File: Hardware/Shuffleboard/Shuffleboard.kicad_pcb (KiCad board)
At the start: 4 copper layers, 131 x 132.4 mm, 31 parts, among them J1 1751138, J2 1751138, U1 COM-09032, U2 PAM8302AAS

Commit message: fet led driving
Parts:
- added D1: Red, LED_THT:LED_D5.0mm, F.Cu at (150.0, 98.5)
- added D32: Green, LED_THT:LED_D5.0mm, F.Cu at (221.2, 28.5)
- added IC1: DG3157EDL-T1-GE3, ShuffleboardFootprints:SOT65P210X110-6N, F.Cu at (157.8, 112.9)
- added IC2: DG3157EDL-T1-GE3, ShuffleboardFootprints:SOT65P210X110-6N, F.Cu at (162.3, 96.9)
- added Q1: NMOS, ShuffleboardFootprints:SOT95P260X110-3N, F.Cu at (145.7, 95.2)
- added R10: 500, Resistor_SMD:R_0603_1608Metric_Pad0.98x0.95mm_HandSolder, F.Cu at (145.8, 98.5)
- added R12: 10k, Resistor_SMD:R_0603_1608Metric_Pad0.98x0.95mm_HandSolder, F.Cu at (158.5, 94.2)
- added R13: 100k, Resistor_SMD:R_0603_1608Metric_Pad0.98x0.95mm_HandSolder, F.Cu at (152.2, 111.8)
- added R45: 10k, Resistor_SMD:R_0603_1608Metric_Pad0.98x0.95mm_HandSolder, F.Cu at (144.8, 114.5)
- added R8: 1k, Resistor_SMD:R_0603_1608Metric_Pad0.98x0.95mm_HandSolder, F.Cu at (227.8, 27.2)
- added R9: 10k, Resistor_SMD:R_0603_1608Metric_Pad0.98x0.95mm_HandSolder, F.Cu at (149.8, 114.5)
- added U3: LMV331, ShuffleboardFootprints:lmv331, F.Cu at (148.8, 108.7)
- J1, J2: value 1751138 -> 1869279; footprint ShuffleboardFootprints:1751138 -> ShuffleboardFootprints:1869279
- moved C6 196.4 mm to (233.2, 32.5), turned to 90 degrees
- moved C2 193.7 mm to (231.0, 32.5), turned to -90 degrees
- moved F1 192.6 mm to (228.8, 32.6), turned to 90 degrees
- moved TP2 190.8 mm to (230.8, 27.8)
- moved R1 158.1 mm to (183.0, 113.8)
- moved R5 151.7 mm to (183.0, 97.3)
- moved C3 145.5 mm to (166.9, 115.0), turned to 180 degrees
- moved R2 141.9 mm to (167.0, 113.0), turned to 180 degrees
- moved C1 140.3 mm to (167.0, 98.0), turned to 180 degrees
- moved R11 135.3 mm to (167.0, 96.0), turned to 180 degrees
- moved C4 118.1 mm to (112.9, 146.2), turned to 180 degrees
- moved J1 117.0 mm to (232.5, 39.8)
- moved R3 110.3 mm to (112.9, 142.9), turned to 180 degrees
- moved C8 109.5 mm to (182.9, 106.5)
- moved R7 109.4 mm to (182.8, 109.8)
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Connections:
- net Net-(U2-OUT+) renamed /Speaker/OUT+
- net Net-(U2-OUT-) renamed /Speaker/OUT-
- C1 pad 1: /PB4SHOOT -> /Inputs/SHOOT_SW
- C2 pad 1: Net-(C2-Pad1) -> +3.3V
- C5 pad 1: /Connector/VER_PB19_ADC1_6 -> /Inputs/VER_POT
- C6 pad 2: Net-(C2-Pad1) -> +3.3V
- F1 pad 2: Net-(C2-Pad1) -> +3.3V
- J1 pad 1: /DACOut -> /3.3VIN
- J1 pad 2: /PB4SHOOT -> /DACOut
- J1 pad 3: /PB1RST -> /PB4SHOOT
- J1 pad 4: /Connector/POS_PB17_ADC1_4 -> /PB1RST
- J1 pad 5: /Connector/HOR_PB18_ADC1_5 -> /Connector/POS_PB17_ADC1_4
- J1 pad 6: /Connector/VER_PB19_ADC1_6 -> /Connector/HOR_PB18_ADC1_5
- J2 pad 1: /3.3VIN -> unconnected-(J2-Pad1)
- J2 pad 6: /Connector/GNDIN -> unconnected-(J2-Pad6)
- R11 pad 2: /PB4SHOOT -> /Inputs/SHOOT_SW
- R4 pad 2: /Connector/VER_PB19_ADC1_6 -> /Inputs/VER_POT
- TP2 pad 1: Net-(C2-Pad1) -> +3.3V
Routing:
- net /Connector/POS_PB17_ADC1_4: track 0.00 -> 171.5 mm, vias 0 -> 1
- net /Connector/HOR_PB18_ADC1_5: track 0.00 -> 114.2 mm, vias 0 -> 1
- net /PB1RST: track 0.00 -> 105.4 mm, vias 0 -> 1
- net /DACOut: track 0.00 -> 102.0 mm, vias 0 -> 1
- net /Connector/VER_PB19_ADC1_6: track 0.00 -> 101.8 mm, vias 0 -> 1
- net /PB4SHOOT: track 0.00 -> 91.2 mm, vias 0 -> 1
- net GND: track 0.00 -> 76.8 mm, vias 0 -> 21
- net +3.3V: track 0.00 -> 50.2 mm, vias 0 -> 13
- net /Inputs/CompOut: track 0.00 -> 46.8 mm
- net /Speaker/OUT+: track 0.00 -> 27.7 mm
- net /Speaker/OUT-: track 0.00 -> 27.7 mm
- net /Inputs/VER_POT: track 0.00 -> 19.7 mm, vias 0 -> 2
- net /Inputs/Vref: track 0.00 -> 17.2 mm
- net /3.3VIN: track 0.00 -> 8.68 mm
- net Net-(C8-Pad1): track 0.00 -> 6.85 mm
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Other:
- board text added: "Rishi Bala Anh-Vu Nguyen"

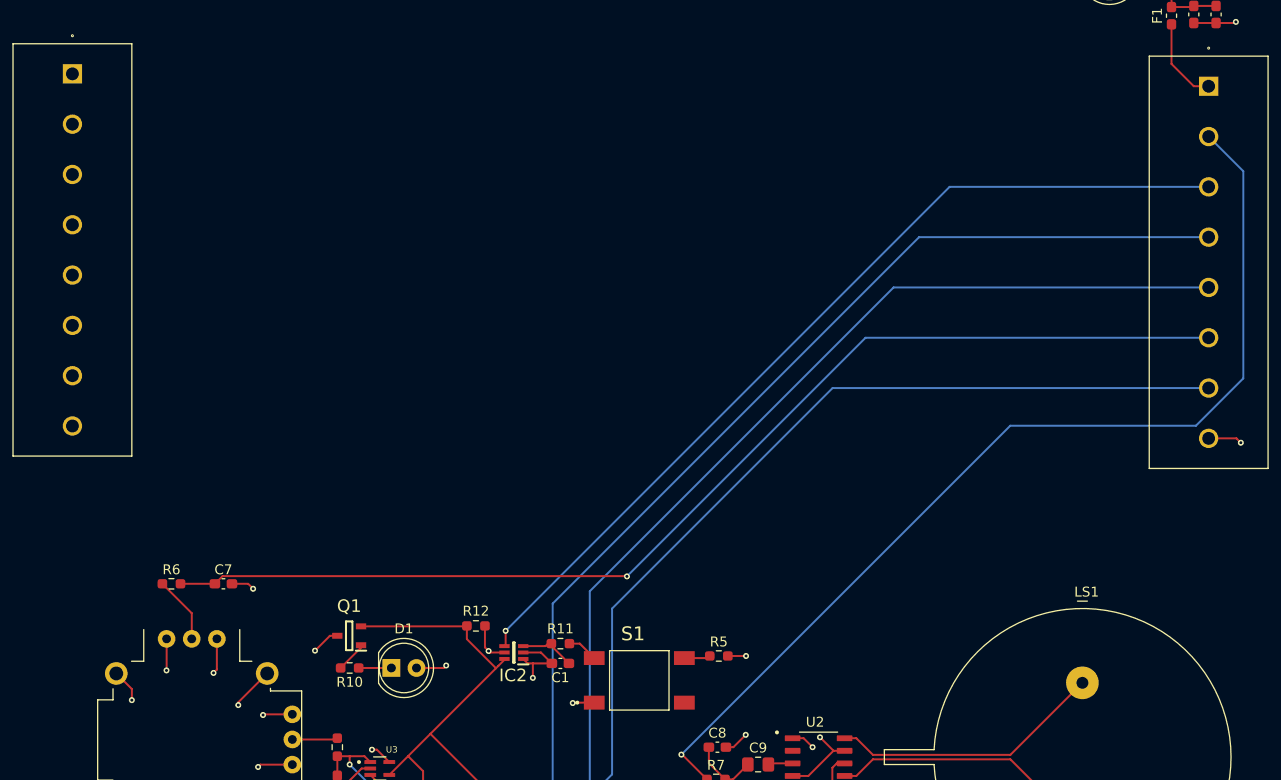
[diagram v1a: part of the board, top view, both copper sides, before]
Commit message: led driving fet
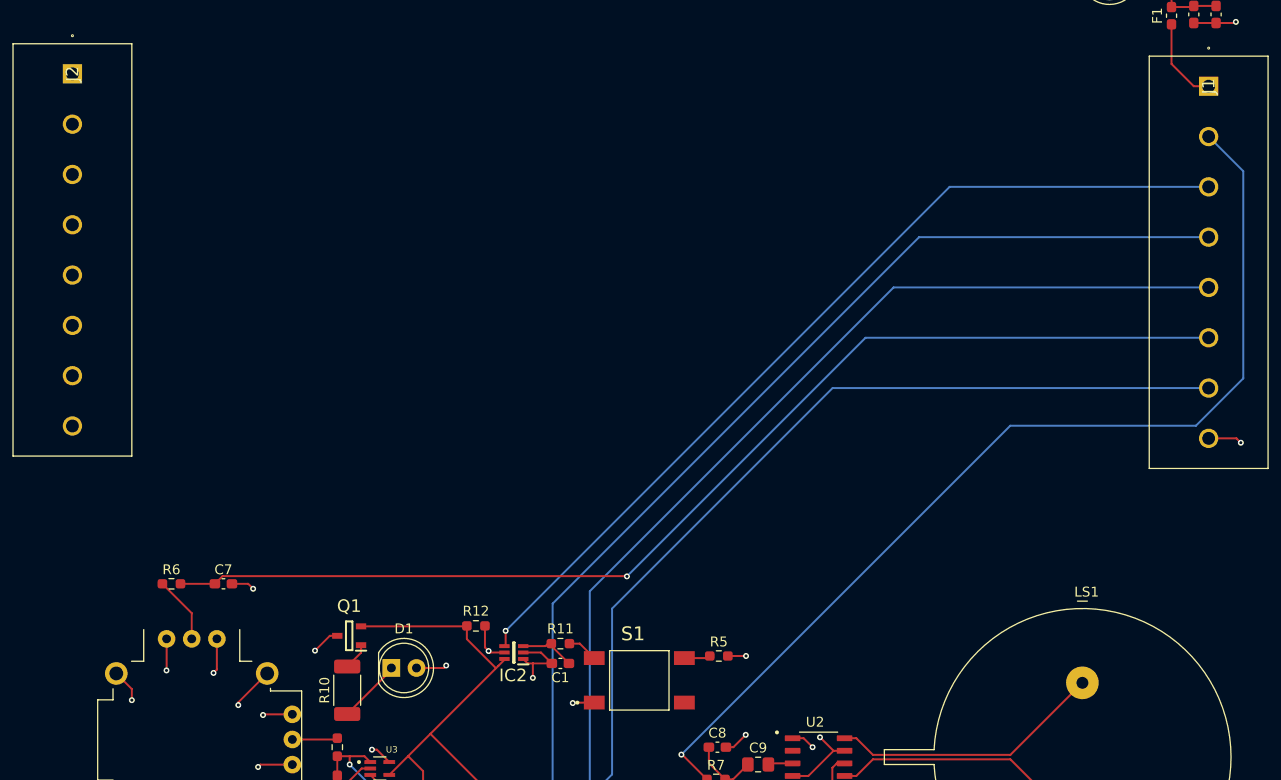
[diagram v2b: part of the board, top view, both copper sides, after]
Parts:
- R10: value 500 -> 330; footprint Resistor_SMD:R_0603_1608Metric_Pad0.98x0.95mm_HandSolder -> Resistor_SMD:R_2010_5025Metric_Pad1.40x2.65mm_HandSolder
- moved R10 2.26 mm to (145.5, 100.8), turned to 90 degrees
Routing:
- net Net-(D1-K): track 3.30 -> 6.50 mm
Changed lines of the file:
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@@
 		)
 	)
-	(footprint "Resistor_SMD:R_0603_1608Metric_Pad0.98x0.95mm_HandSolder"
+	(footprint "Resistor_SMD:R_2010_5025Metric_Pad1.40x2.65mm_HandSolder"
 		(layer "F.Cu")
-		(at 145.75 98.5 180)
-		(descr "Resistor SMD 0603 (1608 Metric), square (rectangular) end terminal, IPC-7351 nominal with elongated pad for handsoldering. (Body size source: IPC-SM-782 page 72, https://www.pcb-3d.com/wordpress/wp-content/uploads/ipc-sm-782a_amendment_1_and_2.pdf), generated with kicad-footprint-generator")
+		(at 145.5 100.75 90)
+		(descr "Resistor SMD 2010 (5025 Metric), square (rectangular) end terminal, IPC-7351 nominal with elongated pad for handsoldering. (Body size source: IPC-SM-782 page 72, https://www.pcb-3d.com/wordpress/wp-content/uploads/ipc-sm-782a_amendment_1_and_2.pdf), generated with kicad-footprint-generator")
 		(tags "resistor handsolder")
 		(property "Reference" "R10"
-			(at 0 -1.43 0)
+			(at 0 -2.28 90)
 			(layer "F.SilkS")
 			(effects
@@
 			)
 		)
-		(property "Value" "500"
-			(at 0 1.43 0)
+		(property "Value" "330"
+			(at 0 2.28 90)
 			(layer "F.Fab")
 			(hide yes)
@@
 		)
 		(property "Datasheet" "~"
-			(at 0 0 0)
+			(at 0 0 90)
 			(layer "F.Fab")
 			(hide yes)
@@
 		)
 		(property "Description" "Resistor"
-			(at 0 0 0)
+			(at 0 0 90)
 			(layer "F.Fab")
 			(hide yes)
@@
 			)
 		)
-		(property "Mouser Link" "https://www.mouser.com/ProductDetail/YAGEO/RE0603DRE07511RL?qs=k2KEx2DUIRRHZePwM2PQsA%3D%3D"
-			(at 0 0 180)
+		(property "Mouser Link" "https://www.mouser.com/ProductDetail/TE-Connectivity-Holsworthy/CRGCQ2010F330R?qs=wUXugUrL1qwW9IDGKnwDXA%3D%3D"
+			(at 0 0 90)
 			(unlocked yes)
 			(layer "F.Fab")
@@
 		)
 		(property "JLCPCB #" ""
-			(at 0 0 180)
+			(at 0 0 90)
 			(unlocked yes)
 			(layer "F.Fab")
@@
 			)
 		)
-		(property "Mouser Part Number" "603-RE0603DRE07511RL"
-			(at 0 0 180)
+		(property "Mouser Part Number" "279-CRGCQ2010F330R"
+			(at 0 0 90)
 			(unlocked yes)
 			(layer "F.Fab")
@@
 		(attr smd)
 		(fp_line
-			(start -0.254724 0.5225)
-			(end 0.254724 0.5225)
+			(start -1.527064 -1.36)
+			(end 1.527064 -1.36)
 			(stroke
 				(width 0.12)
@@
 		)
 		(fp_line
-			(start -0.254724 -0.5225)
-			(end 0.254724 -0.5225)
+			(start -1.527064 1.36)
+			(end 1.527064 1.36)
 			(stroke
 				(width 0.12)
@@
 		)
 		(fp_line
-			(start 1.65 0.73)
-			(end -1.65 0.73)
+			(start 3.35 -1.58)
+			(end 3.35 1.58)
 			(stroke
 				(width 0.05)
@@
 		)
 		(fp_line
-			(start 1.65 -0.73)
-			(end 1.65 0.73)
+			(start -3.35 -1.58)
+			(end 3.35 -1.58)
 			(stroke
 				(width 0.05)
@@
 		)
 		(fp_line
-			(start -1.65 0.73)
-			(end -1.65 -0.73)
+			(start 3.35 1.58)
+			(end -3.35 1.58)
 			(stroke
 				(width 0.05)
@@
 		)
 		(fp_line
-			(start -1.65 -0.73)
-			(end 1.65 -0.73)
+			(start -3.35 1.58)
+			(end -3.35 -1.58)
 			(stroke
 				(width 0.05)
@@
 		)
 		(fp_line
-			(start 0.8 0.4125)
-			(end -0.8 0.4125)
+			(start 2.5 -1.25)
+			(end 2.5 1.25)
 			(stroke
 				(width 0.1)
@@
 		)
 		(fp_line
-			(start 0.8 -0.4125)
-			(end 0.8 0.4125)
+			(start -2.5 -1.25)
+			(end 2.5 -1.25)
 			(stroke
 				(width 0.1)
@@
 		)
 		(fp_line
-			(start -0.8 0.4125)
-			(end -0.8 -0.4125)
+			(start 2.5 1.25)
+			(end -2.5 1.25)
 			(stroke
 				(width 0.1)
@@
 		)
 		(fp_line
-			(start -0.8 -0.4125)
-			(end 0.8 -0.4125)
+			(start -2.5 1.25)
+			(end -2.5 -1.25)
 			(stroke
 				(width 0.1)
@@
 			(layer "F.Fab")
 		)
-		(fp_text user "${REFERENCE}"
-			(at 0 0 0)
-			(layer "F.Fab")
-			(effects
-				(font
-					(size 0.4 0.4)
-					(thickness 0.06)
-				)
-			)
-		)
 		(pad "1" smd roundrect
-			(at -0.9125 0 180)
-			(size 0.975 0.95)
+			(at -2.4 0 90)
+			(size 1.4 2.65)
 			(layers "F.Cu" "F.Mask" "F.Paste")
-			(roundrect_rratio 0.25)
+			(roundrect_rratio 0.178571)
 			(net 39 "Net-(D1-K)")
 			(pintype "passive")
 		)
 		(pad "2" smd roundrect
-			(at 0.9125 0 180)
-			(size 0.975 0.95)
+			(at 2.4 0 90)
+			(size 1.4 2.65)
 			(layers "F.Cu" "F.Mask" "F.Paste")
-			(roundrect_rratio 0.25)
+			(roundrect_rratio 0.178571)
 			(net 40 "Net-(Q1-D)")
 			(pintype "passive")
 		)
 		(embedded_fonts no)
-		(model "${KICAD9_3DMODEL_DIR}/Resistor_SMD.3dshapes/R_0603_1608Metric.step"
+		(model "${KICAD9_3DMODEL_DIR}/Resistor_SMD.3dshapes/R_2010_5025Metric.step"
 			(offset
 				(xyz 0 0 0)
@@
 			(at 0 0 270)
 			(layer "F.SilkS")
-			(hide yes)
 			(effects
 				(font
@@
 			(at 8.045 17.615 0)
 			(layer "F.Fab")
+			(hide yes)
 			(effects
 				(font
@@
 			(at 0 0 270)
 			(layer "F.SilkS")
-			(hide yes)
 			(effects
 				(font
@@
 	)
 	(segment
-		(start 149.96 98.5)
-		(end 146.6625 98.5)
+		(start 145.5 103.15)
+		(end 149.96 98.69)
+		(width 0.2)
+		(layer "F.Cu")
+		(net 39)
+	)
+	(segment
+		(start 149.96 98.69)
+		(end 149.96 98.5)
 		(width 0.2)
 		(layer "F.Cu")
@@
 	)
 	(segment
-		(start 146.9 96.2)
-		(end 146.9 96.4375)
+		(start 146.9 96.95)
+		(end 146.9 96.2)
 		(width 0.2)
 		(layer "F.Cu")
@@
 	)
 	(segment
-		(start 146.9 96.4375)
-		(end 144.8375 98.5)
+		(start 145.5 98.35)
+		(end 146.9 96.95)
 		(width 0.2)
 		(layer "F.Cu")

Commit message: fet driving
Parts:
- added H5: MountingHole, MountingHole:MountingHole_2.2mm_M2, F.Cu at (235.2, 90.0)
- added H6: MountingHole, MountingHole:MountingHole_2.2mm_M2, F.Cu at (113.6, 89.8)
- added J3: Conn_01x10, ShuffleboardFootprints:CES-110-XX-Y-S, F.Cu at (166.1, 41.8)
- moved J2 36.7 mm to (118.0, 75.2), turned to 90 degrees
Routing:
- net GND: track 76.8 -> 75.0 mm

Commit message: repush
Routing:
- net GND: track 75.0 -> 73.7 mm
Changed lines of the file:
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@@
+	)
+	(segment
+		(start 143 95.4)
+		(end 143.6 95.4)
+		(width 0.2)
+		(layer "F.Cu")
+		(net 2)
 	)
 	(segment
@@
 	)
 	(segment
+		(start 143.75 95.25)
+		(end 144.5 95.25)
+		(width 0.2)
+		(layer "F.Cu")
+		(net 2)
+	)
+	(segment
+		(start 143.6 95.4)
+		(end 143.75 95.25)
+		(width 0.2)
+		(layer "F.Cu")
+		(net 2)
+	)
+	(segment
 		(start 122.18 112.3875)
 		(end 124.25 110.3175)
@@
 	)
 	(segment
-		(start 144.5 95.25)
-		(end 143.75 95.25)
-		(width 0.2)
-		(layer "F.Cu")
-		(net 2)
-	)
-	(segment
 		(start 146.9625 108.65)
 		(end 144.5 111.1125)
@@
 	)
 	(segment
-		(start 143.75 95.25)
-		(end 142.25 96.75)
-		(width 0.2)
-		(layer "F.Cu")
-		(net 2)
-	)
-	(segment
 		(start 165.0675 96.94)
 		(end 166.1675 98.04)
@@
 	)
 	(via
-		(at 142.25 96.75)
-		(size 0.6)
-		(drill 0.3)
+		(at 143 95.4)
+		(size 0.6)
+		(drill 0.3)

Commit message: jlc eng fee
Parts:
- moved J2 22.8 mm to (140.8, 76.3)
- moved H2 21.0 mm to (135.5, 28.5)
- moved J1 20.5 mm to (212.0, 39.5)
- moved C2 20.5 mm to (210.5, 32.5)
- moved C6 20.5 mm to (212.8, 32.5)
- moved D32 20.5 mm to (200.7, 28.5)
- moved F1 20.5 mm to (208.2, 32.6)
- moved R8 20.5 mm to (207.2, 27.2)
- moved TP2 20.5 mm to (210.2, 27.8)
- moved H3 19.2 mm to (217.5, 28.5)
- moved J3 9.95 mm to (165.8, 31.8)
- moved H5 1.39 mm to (236.5, 90.5)
- moved H1 0.59 mm to (113.5, 153.0)
- moved H6 0.10 mm to (113.5, 89.8)
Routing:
- net /DACOut: track 102.0 -> 81.5 mm
- net /Connector/HOR_PB18_ADC1_5: track 114.2 -> 93.8 mm
- net /PB4SHOOT: track 91.2 -> 70.8 mm
- net /PB1RST: track 105.4 -> 85.0 mm
- net /Connector/POS_PB17_ADC1_4: track 171.5 -> 151.1 mm
- net /Connector/VER_PB19_ADC1_6: track 101.8 -> 81.4 mm
- net /3.3VIN: track 8.68 -> 7.55 mm
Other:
- board size 131 x 132.4 mm -> 130 x 131.5 mm

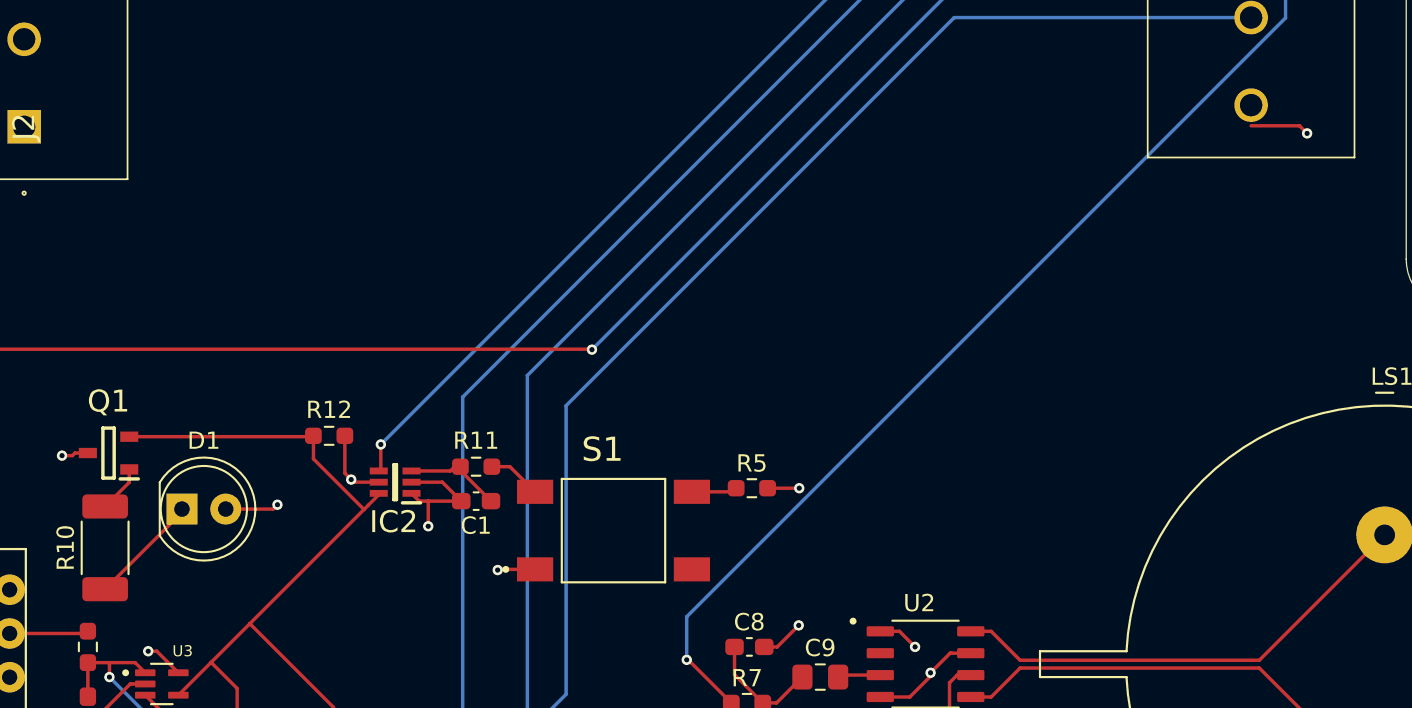
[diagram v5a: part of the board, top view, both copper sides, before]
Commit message: series gate resistor
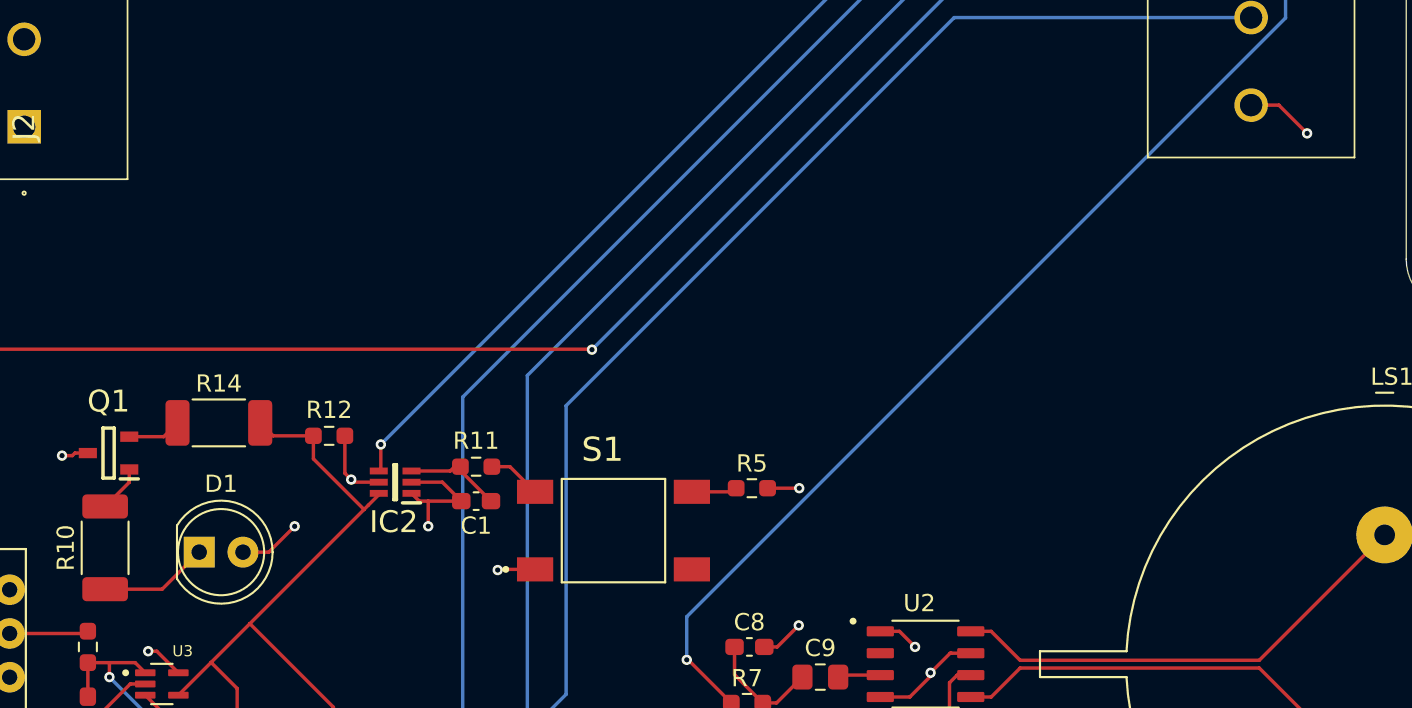
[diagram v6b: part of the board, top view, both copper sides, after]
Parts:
- added R14: 330, Resistor_SMD:R_2010_5025Metric_Pad1.40x2.65mm_HandSolder, F.Cu at (152.1, 93.5)
- moved D1 2.69 mm to (151.0, 101.0)
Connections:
- Q1 pad 2: /Inputs/CompOut -> Net-(Q1-G)
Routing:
- net /Inputs/CompOut: track 46.8 -> 39.6 mm
- net Net-(Q1-G): track 0.00 -> 3.13 mm
